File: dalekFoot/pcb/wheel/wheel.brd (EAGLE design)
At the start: 100.3 x 100 mm, 75 parts, among them IC1 LM1117MP-3.3, IC3 LM1117MP-3.3, IC4 4051D, IC5 4051D, IC6 LM1117MP-3.3, U1 TB6612FNG(O,C,8,EL, U2 SS8050-SOT-23, U3 SS8050-SOT-23, U4 SS8050-SOT-23, U5 TB6612FNG(O,C,8,EL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

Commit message: ready to auto route
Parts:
- moved C7 1.31 mm to (16.5, 60.0), turned to 90 degrees
- moved U2 1.27 mm to (16.5, 64.8)
- moved R29 0.71 mm to (22.2, 60.0), turned to 270 degrees
- moved R32 0.64 mm to (22.2, 64.8), turned to 90 degrees
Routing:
- net BUZZER: track 0.00 -> 30.0 mm
- net LED2: track 0.00 -> 16.8 mm
- net LED1: track 0.00 -> 14.7 mm
- net N$18: track 0.00 -> 7.99 mm
- net N$15: track 0.00 -> 6.50 mm
- net N$11: track 0.00 -> 6.11 mm
- net N$10: track 0.00 -> 6.11 mm
- net N$9: track 0.00 -> 5.71 mm
- net N$17: track 0.00 -> 4.45 mm
- net N$16: track 0.00 -> 4.45 mm
- net N$12: track 0.00 -> 3.25 mm

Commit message: WIP: routing
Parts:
- moved R35 25.1 mm to (90.2, 29.5)
- moved JP5 24.1 mm to (96.5, 36.8)
- moved JP6 22.9 mm to (96.5, 48.3)
- moved JP7 22.9 mm to (96.5, 20.3)
- moved B3 17.5 mm to (86.4, 50.5)
- moved B4 8.96 mm to (78.1, 50.5)
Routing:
- net VCC-IR: track 15.9 -> 195.4 mm, vias 0 -> 2
- net VCC-DIGITAL: track 6.20 -> 175.9 mm
- net VCC-IRT: track 6.20 -> 50.6 mm, vias 0 -> 3
- net DGND: track 281.3 -> 294.6 mm
- net BAT+: track 115.0 -> 126.0 mm
- net BUZZER: track 30.0 -> 22.4 mm
- net BO2.2: track 13.1 -> 14.4 mm
- net BO2.1: track 14.1 -> 15.5 mm
- net BO1.1: track 13.8 -> 15.1 mm
- net AO3.1: track 13.1 -> 14.4 mm
- net BO3.1: track 16.4 -> 17.8 mm
- net AO2.1: track 14.5 -> 15.8 mm
- net AO2.2: track 13.4 -> 14.7 mm
- net BO3.2: track 15.5 -> 16.8 mm
- net AO1.2: track 18.7 -> 19.9 mm
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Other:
- board size 100.3 x 100 mm -> 100 x 100 mm

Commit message: WIP: routing
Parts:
- moved B2 102.8 mm to (28.4, 83.0), turned to 270 degrees
- moved LED1 87.6 mm to (28.1, 91.3)
- moved LED2 85.6 mm to (28.4, 95.6)
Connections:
- net PWM1.B: now also U1.15
- net PWM2.B: no longer U1.15
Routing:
- net DGND: track 294.6 -> 384.4 mm, vias 20 -> 29
- net AIN1.1: track 0.00 -> 26.1 mm, vias 0 -> 1
- net AIN1.2: track 0.00 -> 21.0 mm, vias 0 -> 1
- net PWM1.A: track 0.00 -> 18.9 mm, vias 0 -> 1
- net BIN3.2: track 0.00 -> 17.0 mm, vias 0 -> 1
- net AIN3.2: track 0.00 -> 16.5 mm, vias 0 -> 1
- net BIN2.1: track 0.00 -> 15.9 mm, vias 0 -> 1
- net VCC-IR: track 195.4 -> 180.1 mm, vias 2 -> 5
- net PWM2.A: track 0.00 -> 14.9 mm, vias 0 -> 1
- net PWM1.B: track 0.00 -> 14.0 mm, vias 0 -> 1
- net PWM3.A: track 0.00 -> 12.0 mm, vias 0 -> 1
- net BIN1.1: track 0.00 -> 11.3 mm, vias 0 -> 1
- net AIN3.1: track 0.00 -> 10.7 mm, vias 0 -> 1
- net BIN1.2: track 0.00 -> 10.7 mm, vias 0 -> 1
- net AIN2.2: track 0.00 -> 9.45 mm, vias 0 -> 1
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
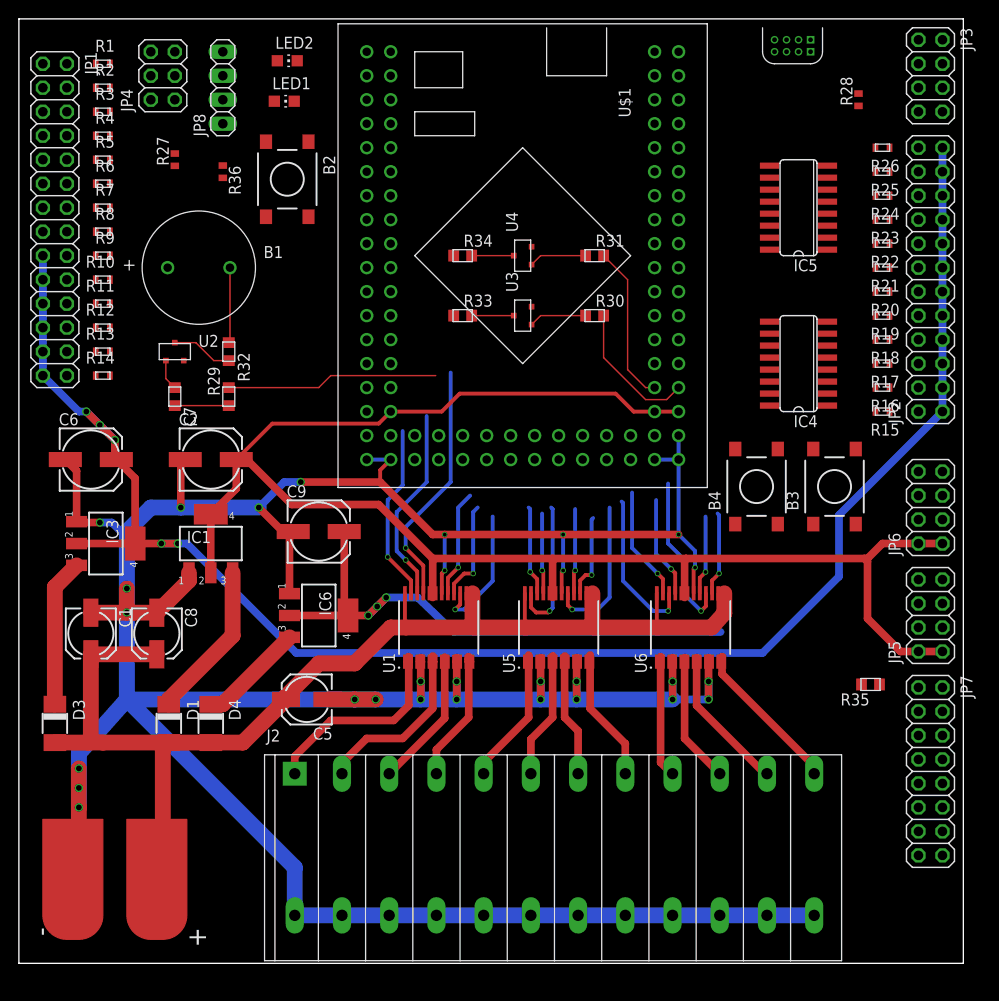
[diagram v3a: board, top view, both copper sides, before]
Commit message: route buttons, leds, encoders
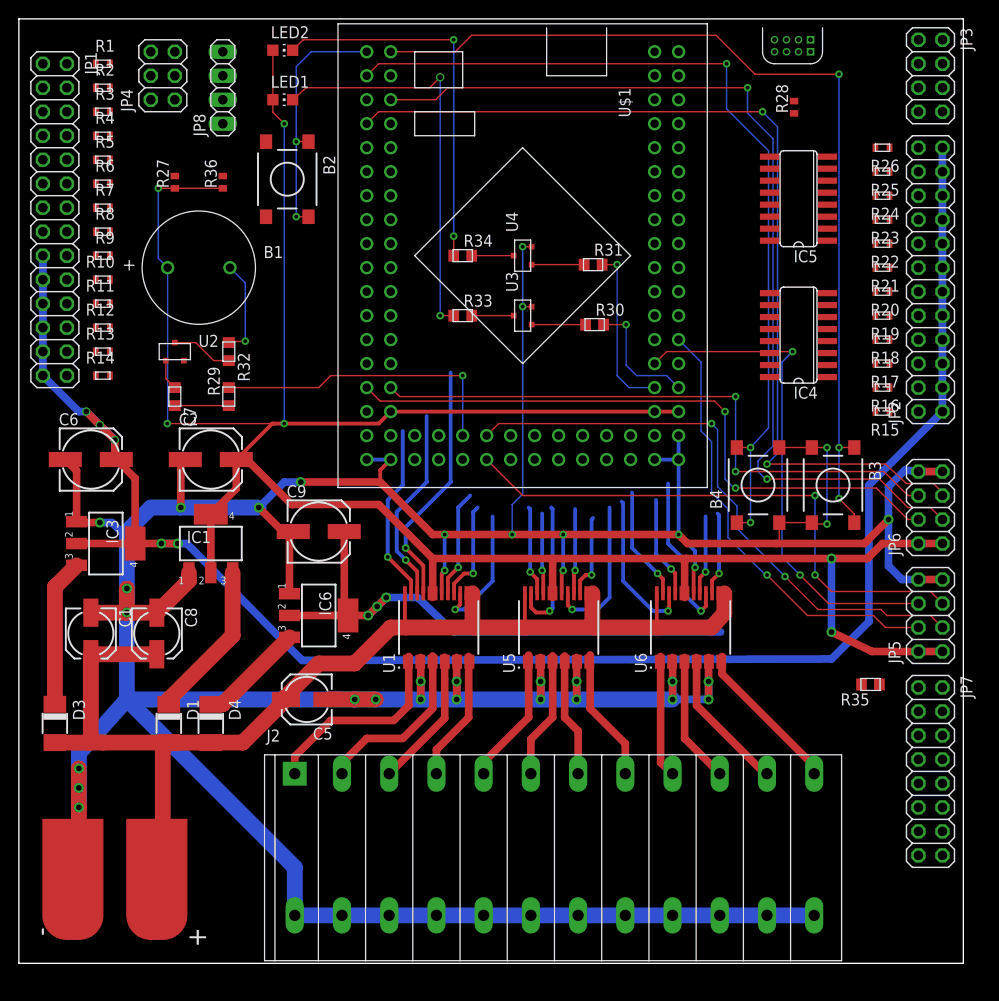
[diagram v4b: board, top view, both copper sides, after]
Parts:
- moved R28 6.87 mm to (82.1, 90.6)
- moved IC4 3.02 mm to (82.5, 66.5)
- moved R27 2.38 mm to (16.5, 82.7)
- moved LED2 1.21 mm to (27.9, 96.7)
- moved R36 1.11 mm to (21.6, 82.7), turned to 90 degrees
- moved R31 0.97 mm to (60.8, 74.0)
- moved IC5 0.95 mm to (82.5, 81.0)
- moved R30 0.95 mm to (61.0, 67.6)
- moved B3 0.22 mm to (86.2, 50.6), turned to 270 degrees
- moved B4 0.22 mm to (78.3, 50.6)
- moved LED1 0.22 mm to (27.9, 91.4)
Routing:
- net DIN1: track 0.00 -> 102.4 mm, vias 0 -> 2
- net DIN2: track 0.00 -> 101.0 mm, vias 0 -> 2
- net BUT2: track 0.00 -> 99.7 mm, vias 0 -> 3
- net DGND: track 384.4 -> 482.8 mm, vias 29 -> 35
- net BUT3: track 0.00 -> 92.7 mm, vias 0 -> 3
- net VCC-DIGITAL: track 175.3 -> 261.4 mm, vias 0 -> 6
- net DIN3: track 0.00 -> 68.4 mm, vias 0 -> 2
- net DIN4: track 0.00 -> 65.3 mm, vias 0 -> 2
- net I2C2_SCL: track 0.00 -> 62.7 mm, vias 0 -> 2
- net I2C2_SDA: track 0.00 -> 59.5 mm, vias 0 -> 2
- net I2C3_SDA: track 0.00 -> 53.8 mm, vias 0 -> 2
- net I2C3_SCL: track 0.00 -> 47.2 mm, vias 0 -> 1
- net N$20: track 0.00 -> 43.2 mm, vias 0 -> 2
- net N$21: track 0.00 -> 40.4 mm, vias 0 -> 2
- net BUT1: track 0.00 -> 26.6 mm, vias 0 -> 2
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
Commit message: routing finished, not tested
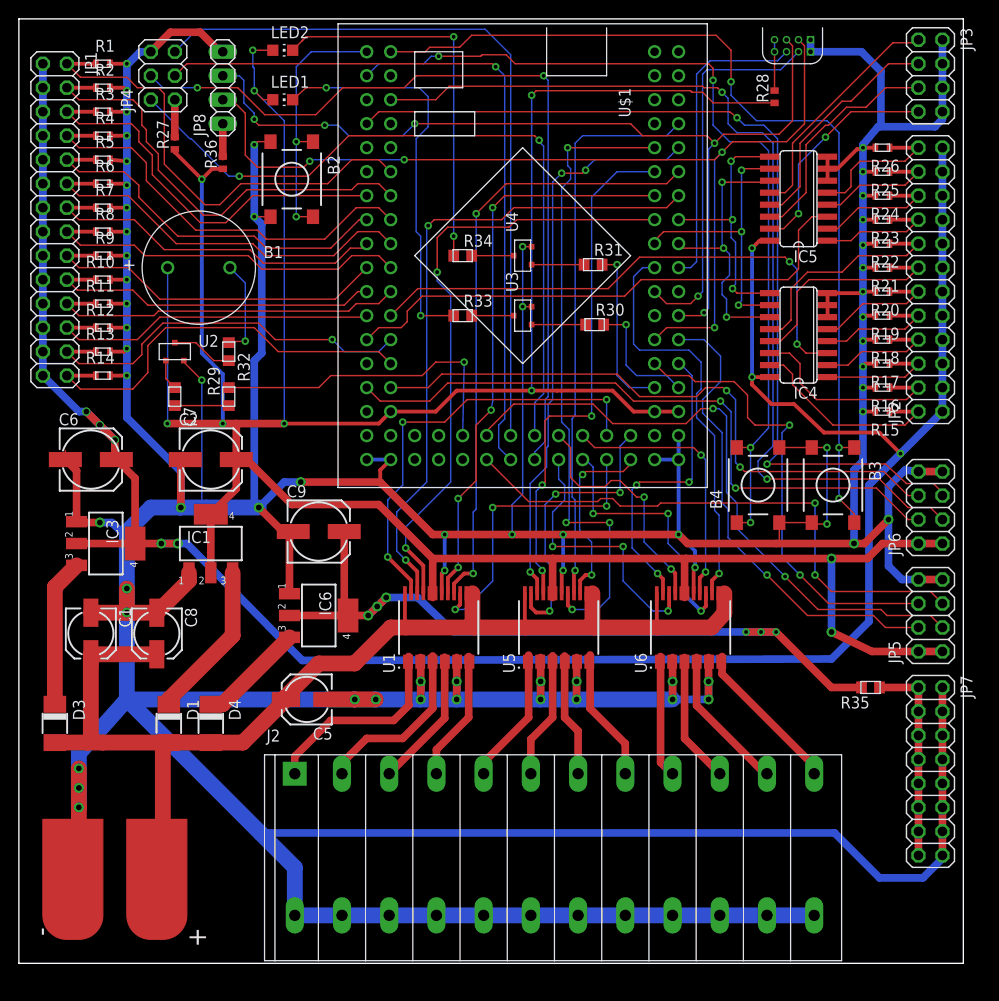
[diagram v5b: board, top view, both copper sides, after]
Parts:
- moved R27 4.13 mm to (16.5, 86.8)
- moved R28 2.34 mm to (80.0, 91.8)
- moved R36 2.06 mm to (21.6, 84.8)
- moved B2 0.48 mm to (28.9, 83.0)
- moved R35 0.32 mm to (90.2, 29.2)
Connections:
- net AIN0: now also IC5.12; no longer IC5.1
- net AIN1: now also IC5.13; no longer IC5.5
- net AIN2: now also IC5.14; no longer IC5.2
- net AIN3: now also IC5.15; no longer IC5.4
- net IR0: now also JP1.8, R4.P$2; no longer JP1.2, R1.P$2
- net IR1: now also JP1.14, R7.P$2; no longer JP1.4, R2.P$2
- net IR10: now also JP1.2, R1.P$2; no longer JP1.22, R11.P$2
- net IR11: now also JP1.6, R3.P$2; no longer JP1.24, R12.P$2
- net IR12: now also JP1.4, R2.P$2; no longer JP1.26, R13.P$2
- net IR13: now also JP1.10, R5.P$2; no longer JP1.28, R14.P$2
- net IR14: now also IC4.15; no longer IC4.13
- net IR16: now also IC4.1; no longer IC4.15
- net IR17: now also IC4.2; no longer IC4.12
- net IR18: now also IC4.4; no longer IC4.1
- net IR2: now also JP1.12, R6.P$2; no longer JP1.6, R3.P$2
- net IR20: now also IC4.13; no longer IC4.2
- net IR21: now also IC4.12; no longer IC4.4
- net IR22: now also IC5.1; no longer IC5.13
- net IR23: now also IC5.2; no longer IC5.14
- net IR24: now also IC5.4; no longer IC5.15
- net IR25: now also IC5.5; no longer IC5.12
- net IR3: now also JP1.18, R9.P$2; no longer JP1.8, R4.P$2
- net IR4: now also JP1.16, R8.P$2; no longer JP1.10, R5.P$2
- net IR5: now also JP1.20, R10.P$2; no longer JP1.12, R6.P$2
- net IR6: now also JP1.22, R11.P$2; no longer JP1.14, R7.P$2
- net IR7: now also JP1.24, R12.P$2; no longer JP1.16, R8.P$2
- net IR8: now also JP1.26, R13.P$2; no longer JP1.18, R9.P$2
- net IR9: now also JP1.28, R14.P$2; no longer JP1.20, R10.P$2
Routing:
- net DGND: track 482.8 -> 829.2 mm, vias 35 -> 65
- net USART_TX: track 0.00 -> 104.0 mm, vias 0 -> 4
- net USART_RX: track 0.00 -> 97.2 mm, vias 0 -> 5
- net SPI_MOSI: track 0.00 -> 86.4 mm, vias 0 -> 2
- net VCC-DIGITAL: track 261.4 -> 342.7 mm, vias 6 -> 10
- net SPI_MISO: track 0.00 -> 78.3 mm, vias 0 -> 2
- net SPI_NSS: track 0.00 -> 78.0 mm
- net SPI_SCK: track 0.00 -> 77.4 mm, vias 0 -> 1
- net PC4_AIN: track 0.00 -> 57.7 mm, vias 0 -> 2
- net VCC-IR: track 185.4 -> 242.9 mm, vias 5 -> 8
- net PC5_AIN: track 0.00 -> 57.3 mm
- net BIN1.2: track 10.7 -> 65.0 mm, vias 1 -> 2
- net BIN2.1: track 15.9 -> 68.8 mm, vias 1 -> 4
- net IR10: track 0.00 -> 52.8 mm
- net BIN2.2: track 8.97 -> 59.7 mm
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
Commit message: routing finished
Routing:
- net VCC-DIGITAL: track 342.7 -> 333.2 mm
- net I2C2_SCL: track 67.4 -> 64.4 mm
- net BUT3: track 94.2 -> 96.7 mm
- net I2C3_SDA: track 49.2 -> 46.9 mm
- net BAT+: track 126.5 -> 128.4 mm
- net BUT2: track 98.8 -> 96.9 mm
- net BO1.2: track 14.8 -> 15.9 mm
- net DIN1: track 102.2 -> 103.3 mm
- net USART_RX: track 97.2 -> 96.2 mm
- net DGND: track 829.2 -> 828.3 mm
